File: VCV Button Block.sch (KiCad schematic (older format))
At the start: 18 parts, among them J17 Conn_01x08_Female, SW41 SW_SPST_4_PIN, SW42 SW_SPST_4_PIN, SW43 SW_SPST_4_PIN, SW44 SW_SPST_4_PIN, SW45 SW_SPST_4_PIN, SW46 SW_SPST_4_PIN, SW47 SW_SPST_4_PIN, SW48 SW_SPST_4_PIN, SW49 SW_SPST_4_PIN, SW50 SW_SPST_4_PIN, SW51 SW_SPST_4_PIN, SW52 SW_SPST_4_PIN, SW53 SW_SPST_4_PIN, SW54 SW_SPST_4_PIN, SW55 SW_SPST_4_PIN, SW56 SW_SPST_4_PIN, U4 CD74HC4067M

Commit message: Beginning button connections
Beginning running traces to the button blocks modified schematic to ensure minimum trace length, rotate buttons to achieve this.
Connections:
- wire segments 114 -> 116
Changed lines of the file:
@@
 	3800 1900 5100 1900
 Wire Wire Line
-	5300 1800 5300 3150
-Wire Wire Line
-	5400 1750 5400 2650
-Wire Wire Line
-	5500 1700 5500 2150
-Wire Wire Line
-	5500 2150 5650 2150
-Wire Wire Line
-	2950 1650 5650 1650
-Wire Wire Line
-	5400 2650 5650 2650
-Wire Wire Line
-	5300 3150 5650 3150
+	2950 1650 5600 1650
 Wire Wire Line
 	3400 1700 5500 1700
@@
 Wire Wire Line
 	2450 1050 2450 1250
-NoConn ~ 5650 1750
-NoConn ~ 5650 2250
-NoConn ~ 5650 2750
-NoConn ~ 5650 3250
 NoConn ~ 5650 4750
 NoConn ~ 6050 5250
@@
 	5650 4650 5000 4650
 Wire Wire Line
-	4900 5250 5650 5250
-Wire Wire Line
-	4900 2000 4900 5250
-Wire Wire Line
-	5100 4250 5650 4250
-Wire Wire Line
-	5100 1900 5100 4250
-Wire Wire Line
-	5200 3750 5650 3750
+	4900 2000 4900 5150
+Wire Wire Line
+	5100 1900 5100 4150
 Wire Wire Line
 	4000 3050 4150 3050
@@
 NoConn ~ 4150 2950
 NoConn ~ 4150 2450
-NoConn ~ 5650 3650
-NoConn ~ 5650 4150
-NoConn ~ 5650 5150
-Wire Wire Line
-	5200 1850 5200 3750
+Wire Wire Line
+	5200 1850 5200 3650
+Wire Wire Line
+	5650 4150 5100 4150
+NoConn ~ 5650 4250
+Wire Wire Line
+	5600 1650 5600 1750
+Wire Wire Line
+	5600 1750 5650 1750
+NoConn ~ 5650 1650
+Wire Wire Line
+	5650 5150 4900 5150
+NoConn ~ 5650 5250
+Wire Wire Line
+	5500 2250 5650 2250
+Wire Wire Line
+	5500 1700 5500 2250
+NoConn ~ 5650 2150
+Wire Wire Line
+	5650 3650 5200 3650
+Wire Wire Line
+	5650 3250 5300 3250
+Wire Wire Line
+	5300 1800 5300 3250
+Wire Wire Line
+	5650 2750 5400 2750
+Wire Wire Line
+	5400 1750 5400 2750
+NoConn ~ 5650 3750
+NoConn ~ 5650 3150
+NoConn ~ 5650 2650
 $EndSCHEMATC

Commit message: Further work on the separate boards
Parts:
- SW41, SW42, SW43, SW44, SW45, SW46, SW47, SW48, SW49, SW50, SW51, SW52, SW53, SW54, SW55, SW56: symbol sw_spst_0:SW_SPST_4_PIN -> cp_midi_control_surface_002-rescue:SW_SPST_4_PIN-sw_spst_0
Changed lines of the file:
@@
 $EndDescr
 $Comp
-L sw_spst_0:SW_SPST_4_PIN SW?
+L cp_midi_control_surface_002-rescue:SW_SPST_4_PIN-sw_spst_0 SW?
 U 1 1 5C60FAD2
 P 5850 1650
 AR Path="/5C4B73B3/5C60FAD2" Ref="SW?"  Part="1"
 AR Path="/5C4BAA18/5C60FAD2" Ref="SW41"  Part="1"
+AR Path="/5C60FAD2" Ref="SW41"  Part="1"
 F 0 "SW41" H 5850 1400 50  0000 C CNN
 F 1 "SW_SPST_4_PIN" H 5850 1824 50  0001 C CNN
@@
 $EndComp
 $Comp
-L sw_spst_0:SW_SPST_4_PIN SW?
+L cp_midi_control_surface_002-rescue:SW_SPST_4_PIN-sw_spst_0 SW?
 U 1 1 5C60FAD9
 P 5850 2150
 AR Path="/5C4B73B3/5C60FAD9" Ref="SW?"  Part="1"
 AR Path="/5C4BAA18/5C60FAD9" Ref="SW42"  Part="1"
+AR Path="/5C60FAD9" Ref="SW42"  Part="1"
 F 0 "SW42" H 5850 1950 50  0000 C CNN
 F 1 "SW_SPST_4_PIN" H 5850 2324 50  0001 C CNN
@@
 $EndComp
 $Comp
-L sw_spst_0:SW_SPST_4_PIN SW?
+L cp_midi_control_surface_002-rescue:SW_SPST_4_PIN-sw_spst_0 SW?
 U 1 1 5C60FAE0
 P 5850 2650
 AR Path="/5C4B73B3/5C60FAE0" Ref="SW?"  Part="1"
 AR Path="/5C4BAA18/5C60FAE0" Ref="SW43"  Part="1"
+AR Path="/5C60FAE0" Ref="SW43"  Part="1"
 F 0 "SW43" H 5850 2450 50  0000 C CNN
 F 1 "SW_SPST_4_PIN" H 5850 2824 50  0001 C CNN
@@
 $EndComp
 $Comp
-L sw_spst_0:SW_SPST_4_PIN SW?
+L cp_midi_control_surface_002-rescue:SW_SPST_4_PIN-sw_spst_0 SW?
 U 1 1 5C60FAE7
 P 5850 3150
 AR Path="/5C4B73B3/5C60FAE7" Ref="SW?"  Part="1"
 AR Path="/5C4BAA18/5C60FAE7" Ref="SW44"  Part="1"
+AR Path="/5C60FAE7" Ref="SW44"  Part="1"
 F 0 "SW44" H 5850 2950 50  0000 C CNN
 F 1 "SW_SPST_4_PIN" H 5850 3324 50  0001 C CNN
@@
 $EndComp
 $Comp
-L sw_spst_0:SW_SPST_4_PIN SW?
+L cp_midi_control_surface_002-rescue:SW_SPST_4_PIN-sw_spst_0 SW?
 U 1 1 5C60FAEE
 P 5850 3650
 AR Path="/5C4B73B3/5C60FAEE" Ref="SW?"  Part="1"
 AR Path="/5C4BAA18/5C60FAEE" Ref="SW45"  Part="1"
+AR Path="/5C60FAEE" Ref="SW45"  Part="1"
 F 0 "SW45" H 5850 3450 50  0000 C CNN
 F 1 "SW_SPST_4_PIN" H 5850 3824 50  0001 C CNN
@@
 $EndComp
 $Comp
-L sw_spst_0:SW_SPST_4_PIN SW?
+L cp_midi_control_surface_002-rescue:SW_SPST_4_PIN-sw_spst_0 SW?
 U 1 1 5C60FAF5
 P 5850 4150
 AR Path="/5C4B73B3/5C60FAF5" Ref="SW?"  Part="1"
 AR Path="/5C4BAA18/5C60FAF5" Ref="SW46"  Part="1"
+AR Path="/5C60FAF5" Ref="SW46"  Part="1"
 F 0 "SW46" H 5850 3950 50  0000 C CNN
 F 1 "SW_SPST_4_PIN" H 5850 4324 50  0001 C CNN
@@
 $EndComp
 $Comp
-L sw_spst_0:SW_SPST_4_PIN SW?
+L cp_midi_control_surface_002-rescue:SW_SPST_4_PIN-sw_spst_0 SW?
 U 1 1 5C60FAFC
 P 5850 4650
 AR Path="/5C4B73B3/5C60FAFC" Ref="SW?"  Part="1"
 AR Path="/5C4BAA18/5C60FAFC" Ref="SW47"  Part="1"
+AR Path="/5C60FAFC" Ref="SW47"  Part="1"
 F 0 "SW47" H 5850 4450 50  0000 C CNN
 F 1 "SW_SPST_4_PIN" H 5850 4824 50  0001 C CNN
@@
 $EndComp
 $Comp
-L sw_spst_0:SW_SPST_4_PIN SW?
+L cp_midi_control_surface_002-rescue:SW_SPST_4_PIN-sw_spst_0 SW?
 U 1 1 5C60FB03
 P 5850 5150
 AR Path="/5C4B73B3/5C60FB03" Ref="SW?"  Part="1"
 AR Path="/5C4BAA18/5C60FB03" Ref="SW48"  Part="1"
+AR Path="/5C60FB03" Ref="SW48"  Part="1"
 F 0 "SW48" H 5850 4950 50  0000 C CNN
 F 1 "SW_SPST_4_PIN" H 5850 5324 50  0001 C CNN
@@
 $EndComp
 $Comp
-L sw_spst_0:SW_SPST_4_PIN SW?
+L cp_midi_control_surface_002-rescue:SW_SPST_4_PIN-sw_spst_0 SW?
 U 1 1 5C60FB0A
 P 4350 2450
 AR Path="/5C4B73B3/5C60FB0A" Ref="SW?"  Part="1"
 AR Path="/5C4BAA18/5C60FB0A" Ref="SW49"  Part="1"
+AR Path="/5C60FB0A" Ref="SW49"  Part="1"
 F 0 "SW49" H 4350 2250 50  0000 C CNN
 F 1 "SW_SPST_4_PIN" H 5050 2400 50  0001 C CNN
@@
 $EndComp
 $Comp
-L sw_spst_0:SW_SPST_4_PIN SW?
+L cp_midi_control_surface_002-rescue:SW_SPST_4_PIN-sw_spst_0 SW?
 U 1 1 5C60FB11
 P 4350 2950
 AR Path="/5C4B73B3/5C60FB11" Ref="SW?"  Part="1"
 AR Path="/5C4BAA18/5C60FB11" Ref="SW50"  Part="1"
+AR Path="/5C60FB11" Ref="SW50"  Part="1"
 F 0 "SW50" H 4350 2750 50  0000 C CNN
 F 1 "SW_SPST_4_PIN" H 4350 3124 50  0001 C CNN
@@
 $EndComp
 $Comp
-L sw_spst_0:SW_SPST_4_PIN SW?
+L cp_midi_control_surface_002-rescue:SW_SPST_4_PIN-sw_spst_0 SW?
 U 1 1 5C60FB1F
 P 4350 3950
 AR Path="/5C4B73B3/5C60FB1F" Ref="SW?"  Part="1"
 AR Path="/5C4BAA18/5C60FB1F" Ref="SW52"  Part="1"
+AR Path="/5C60FB1F" Ref="SW52"  Part="1"
 F 0 "SW52" H 4350 3750 50  0000 C CNN
 F 1 "SW_SPST_4_PIN" H 4350 4124 50  0001 C CNN
@@
 $EndComp
 $Comp
-L sw_spst_0:SW_SPST_4_PIN SW?
+L cp_midi_control_surface_002-rescue:SW_SPST_4_PIN-sw_spst_0 SW?
 U 1 1 5C60FB26
 P 4350 4450
 AR Path="/5C4B73B3/5C60FB26" Ref="SW?"  Part="1"
 AR Path="/5C4BAA18/5C60FB26" Ref="SW53"  Part="1"
+AR Path="/5C60FB26" Ref="SW53"  Part="1"
 F 0 "SW53" H 4350 4250 50  0000 C CNN
 F 1 "SW_SPST_4_PIN" H 4350 4624 50  0001 C CNN
@@
 $EndComp
 $Comp
-L sw_spst_0:SW_SPST_4_PIN SW?
+L cp_midi_control_surface_002-rescue:SW_SPST_4_PIN-sw_spst_0 SW?
 U 1 1 5C60FB2D
 P 4350 4950
 AR Path="/5C4B73B3/5C60FB2D" Ref="SW?"  Part="1"
 AR Path="/5C4BAA18/5C60FB2D" Ref="SW54"  Part="1"
+AR Path="/5C60FB2D" Ref="SW54"  Part="1"
 F 0 "SW54" H 4350 4750 50  0000 C CNN
 F 1 "SW_SPST_4_PIN" H 4350 5124 50  0001 C CNN
@@
 $EndComp
 $Comp
-L sw_spst_0:SW_SPST_4_PIN SW?
+L cp_midi_control_surface_002-rescue:SW_SPST_4_PIN-sw_spst_0 SW?
 U 1 1 5C60FB34
 P 4350 5450
 AR Path="/5C4B73B3/5C60FB34" Ref="SW?"  Part="1"
 AR Path="/5C4BAA18/5C60FB34" Ref="SW55"  Part="1"
+AR Path="/5C60FB34" Ref="SW55"  Part="1"
 F 0 "SW55" H 4350 5250 50  0000 C CNN
 F 1 "SW_SPST_4_PIN" H 4350 5624 50  0001 C CNN
@@
 $EndComp
 $Comp
-L sw_spst_0:SW_SPST_4_PIN SW?
+L cp_midi_control_surface_002-rescue:SW_SPST_4_PIN-sw_spst_0 SW?
 U 1 1 5C60FB3B
 P 4350 5950
 AR Path="/5C4B73B3/5C60FB3B" Ref="SW?"  Part="1"
 AR Path="/5C4BAA18/5C60FB3B" Ref="SW56"  Part="1"
+AR Path="/5C60FB3B" Ref="SW56"  Part="1"
 F 0 "SW56" H 4350 5750 50  0000 C CNN
 F 1 "SW_SPST_4_PIN" H 4350 6124 50  0001 C CNN
@@
 Connection ~ 1950 3550
 $Comp
-L sw_spst_0:SW_SPST_4_PIN SW?
+L cp_midi_control_surface_002-rescue:SW_SPST_4_PIN-sw_spst_0 SW?
 U 1 1 5C60FB18
 P 4350 3450
 AR Path="/5C4B73B3/5C60FB18" Ref="SW?"  Part="1"
 AR Path="/5C4BAA18/5C60FB18" Ref="SW51"  Part="1"
+AR Path="/5C60FB18" Ref="SW51"  Part="1"
 F 0 "SW51" H 4350 3250 50  0000 C CNN
 F 1 "SW_SPST_4_PIN" H 4350 3624 50  0001 C CNN

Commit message: Sub boards completed
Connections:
- net at U4.13 (S3): now also J17.3 (Pin_3); no longer J17.4 (Pin_4)
- net at U4.14 (S2): now also J17.4 (Pin_4); no longer J17.3 (Pin_3)
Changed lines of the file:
@@
 NoConn ~ 1000 2950
-Wire Wire Line
-	1000 2550 1950 2550
 Wire Wire Line
 	1000 2250 1950 2250
 Wire Wire Line
 	1000 2350 1950 2350
-Wire Wire Line
-	1000 2450 1950 2450
 Wire Wire Line
 	1650 2650 1650 1850
@@
 NoConn ~ 5650 3150
 NoConn ~ 5650 2650
+Wire Wire Line
+	1000 2450 1350 2450
+Wire Wire Line
+	1350 2450 1350 2550
+Wire Wire Line
+	1350 2550 1950 2550
+Wire Wire Line
+	1950 2450 1950 2500
+Wire Wire Line
+	1950 2500 1000 2500
+Wire Wire Line
+	1000 2500 1000 2550
 $EndSCHEMATC

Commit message: Tidy schematic / renumber components / complete daughter boards
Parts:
- J7: renamed from J17; value Conn_01x08_Female -> ~; symbol Connector:Conn_01x08_Female -> Connector:Conn_01x08_Male
- SW41, SW42, SW43, SW44, SW45, SW46, SW47, SW48, SW49, SW50, SW51, SW52, SW53, SW54, SW55, SW56: value SW_SPST_4_PIN -> B3F-5050
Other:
- moved on the sheet: SW41, SW42, SW43, SW44, SW45, SW46, SW47, SW48, SW49, SW50, SW51, SW52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

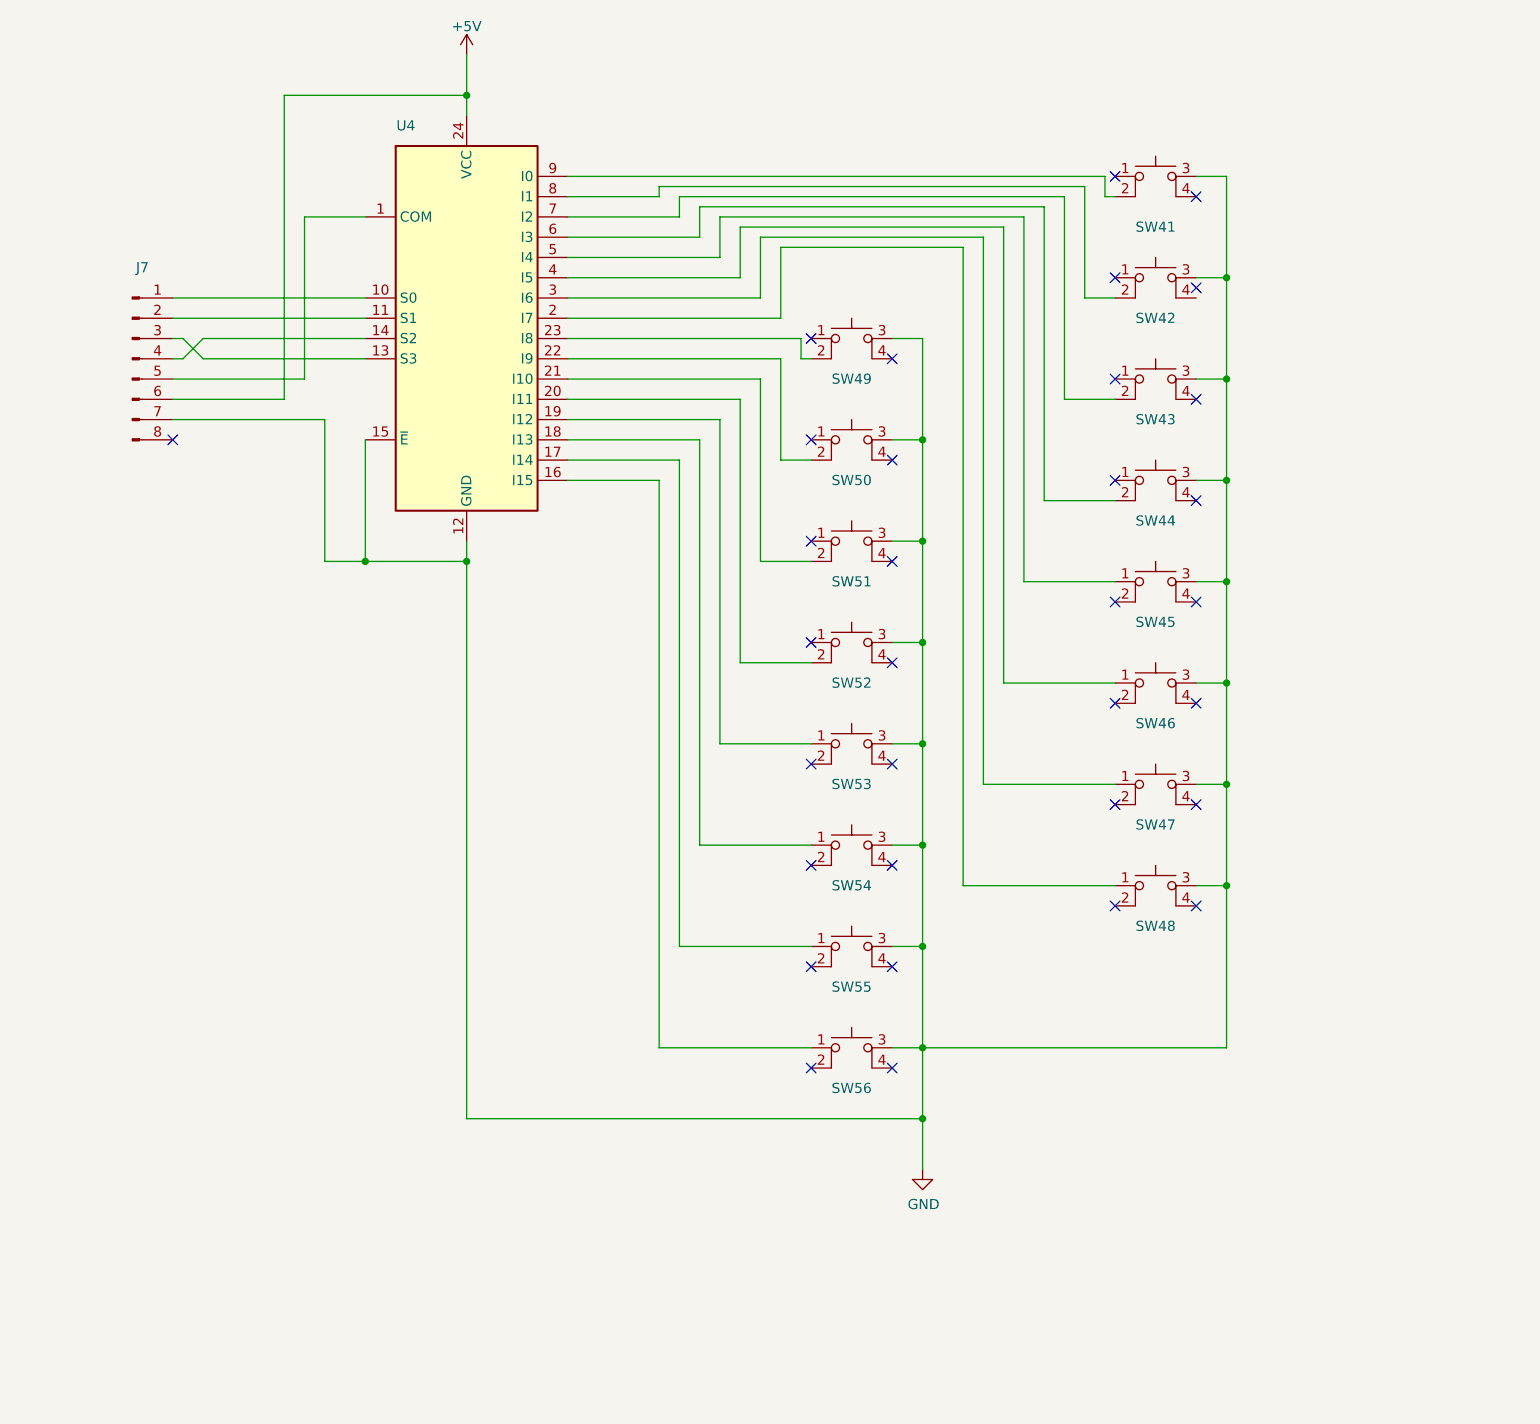
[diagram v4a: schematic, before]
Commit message: Redesign of upper boards
Added bussed resistors following Igor's correction to the schematic + tidied schematic.
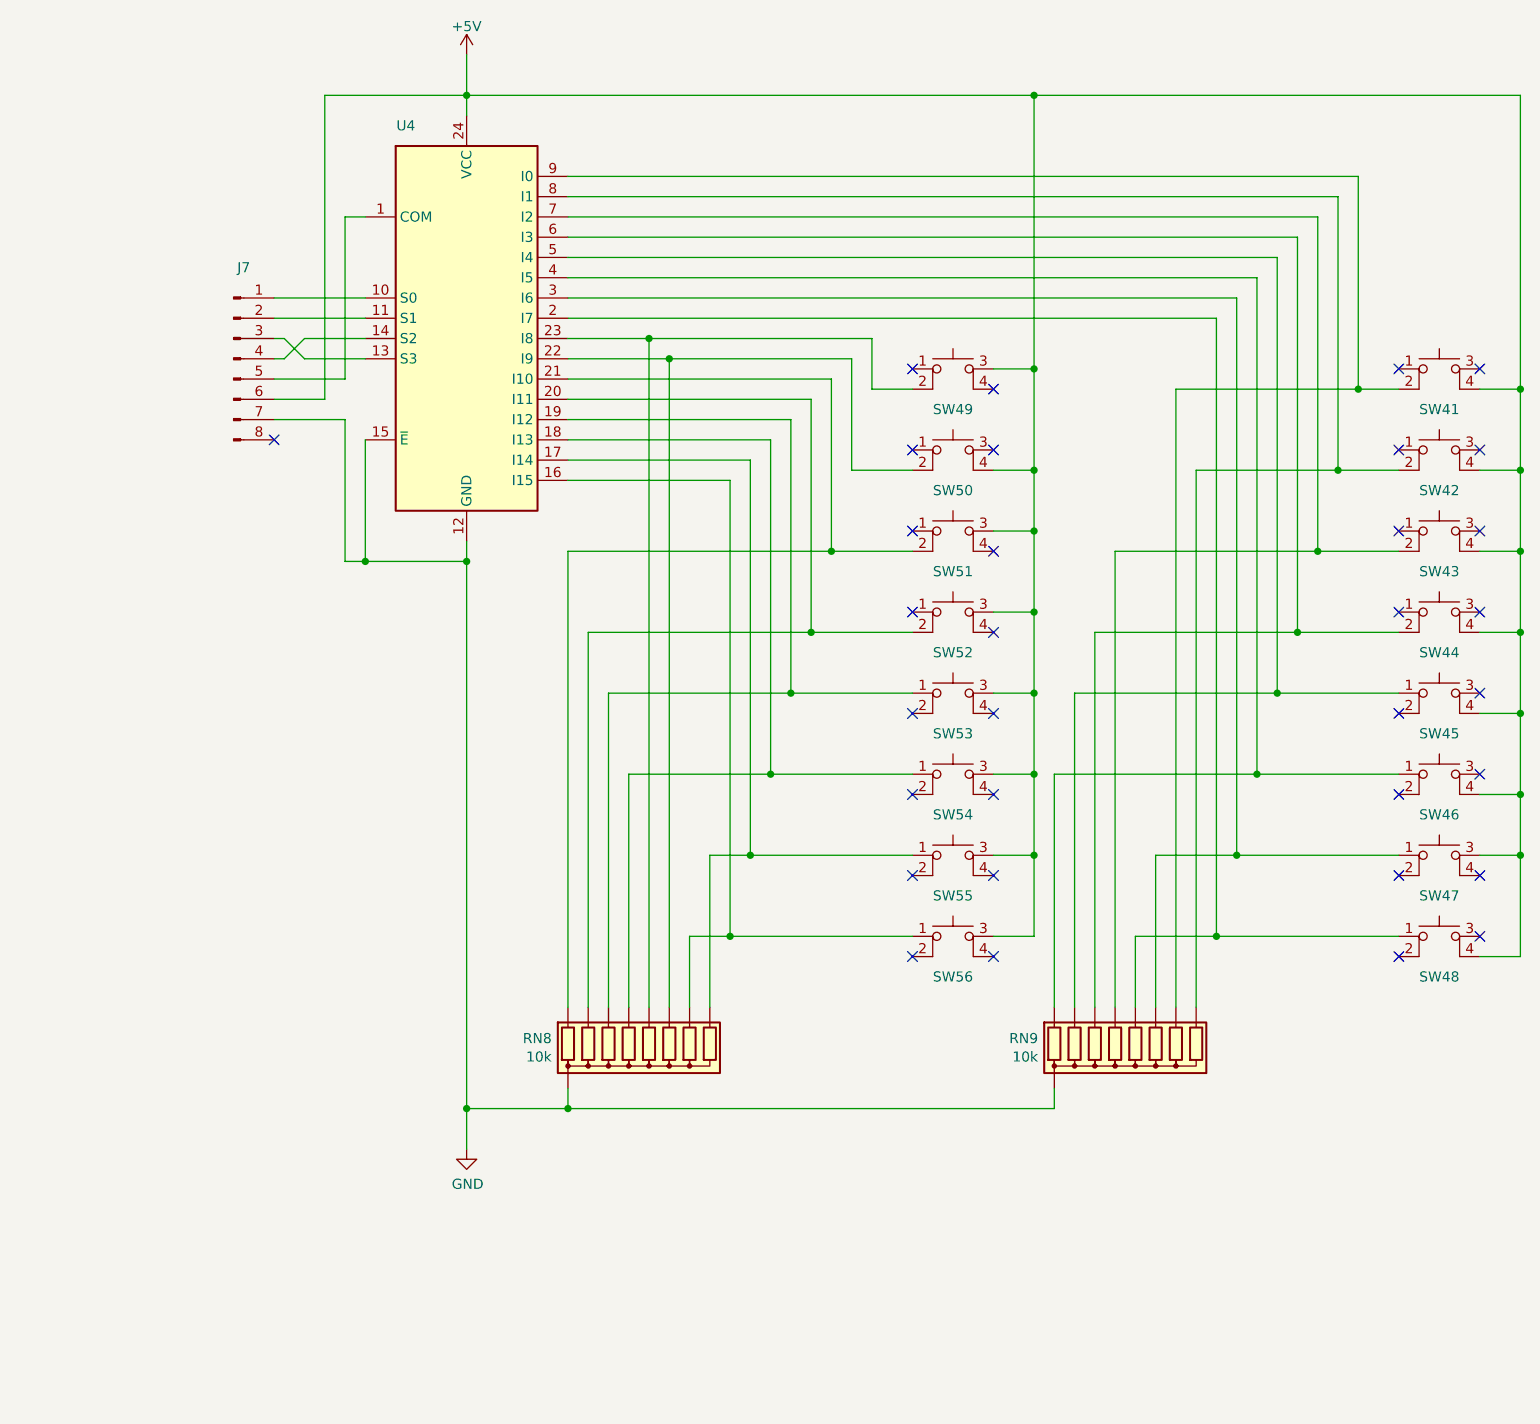
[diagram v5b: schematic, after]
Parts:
- added RN8, RN9: 10k, Resistor_THT:R_Array_SIP9, symbol Device:R_Network08
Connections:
- net +5V: now also SW41.4, SW42.4, SW43.4, SW44.4, SW45.4, SW46.4, SW47.3, SW48.4, SW49.3, SW50.4, SW51.3, SW52.3, SW53.3, SW54.3, SW55.3, SW56.3
- net GND: now also RN8.1 (common), RN9.1 (common); no longer SW41.3, SW42.3, SW43.3, SW44.3, SW45.3, SW46.3, SW47.3, SW48.3, SW49.3, SW50.3, SW51.3, SW52.3, SW53.3, SW54.3, SW55.3, SW56.3
- net at SW41.2, U4.9 (I0): now also RN9.8 (R7)
- net at SW42.2, U4.8 (I1): now also RN9.9 (R8)
- net at SW43.2, U4.7 (I2): now also RN9.5 (R4)
- net at SW44.2, U4.6 (I3): now also RN9.4 (R3)
- net at SW45.1 (A), U4.5 (I4): now also RN9.3 (R2)
- net at SW46.1 (A), U4.4 (I5): now also RN9.2 (R1)
- net at SW47.1 (A), U4.3 (I6): now also RN9.7 (R6)
- net at SW48.1 (A), U4.2 (I7): now also RN9.6 (R5)
- net at SW49.2, U4.23 (I8): now also RN8.6 (R5)
- net at SW50.2, U4.22 (I9): now also RN8.7 (R6)
- net at SW51.2, U4.21 (I10): now also RN8.2 (R1)
- net at SW52.2, U4.20 (I11): now also RN8.3 (R2)
- net at SW53.1 (A), U4.19 (I12): now also RN8.4 (R3)
- net at SW54.1 (A), U4.18 (I13): now also RN8.5 (R4)
- net at SW55.1 (A), U4.17 (I14): now also RN8.9 (R8)
- net at SW56.1 (A), U4.16 (I15): now also RN8.8 (R7)
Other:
- moved on the sheet: J7, SW41, SW42, SW43, SW44, SW45, SW46, SW47, SW48, SW49, SW50, SW51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
